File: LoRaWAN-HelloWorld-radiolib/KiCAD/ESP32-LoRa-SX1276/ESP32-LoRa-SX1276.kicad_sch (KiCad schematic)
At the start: 2 parts, among them U1 ESP32-DEVKITC-32UE, U2 SX1276

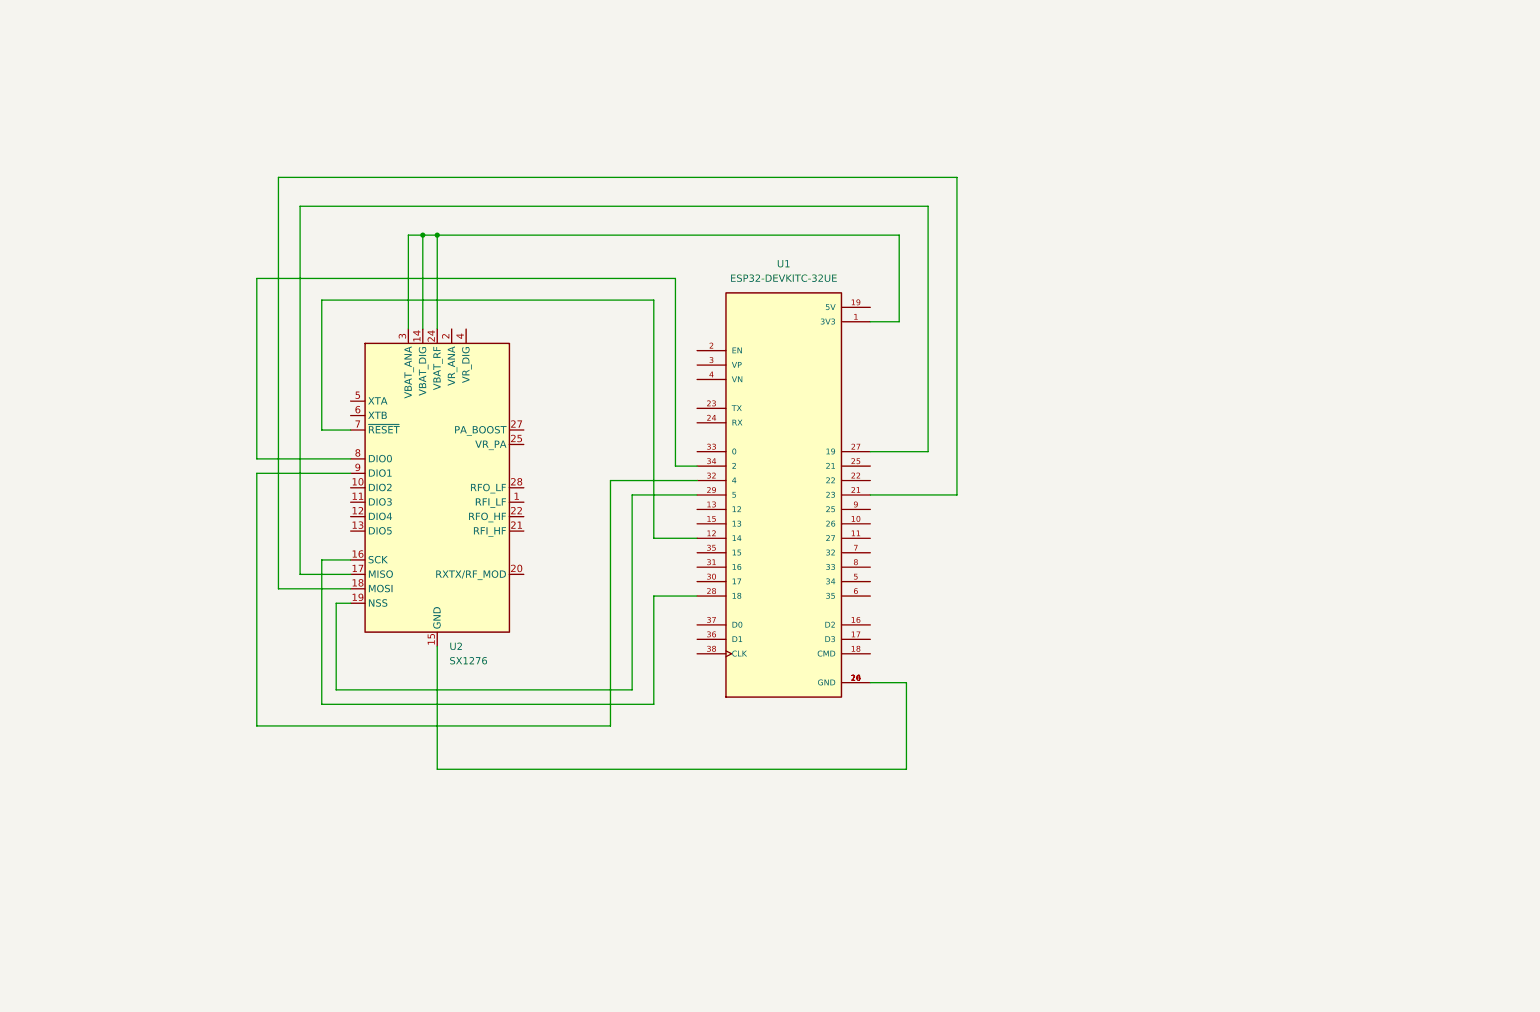
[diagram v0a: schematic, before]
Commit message: Roll back to full schema for SX1276 including all other sensors
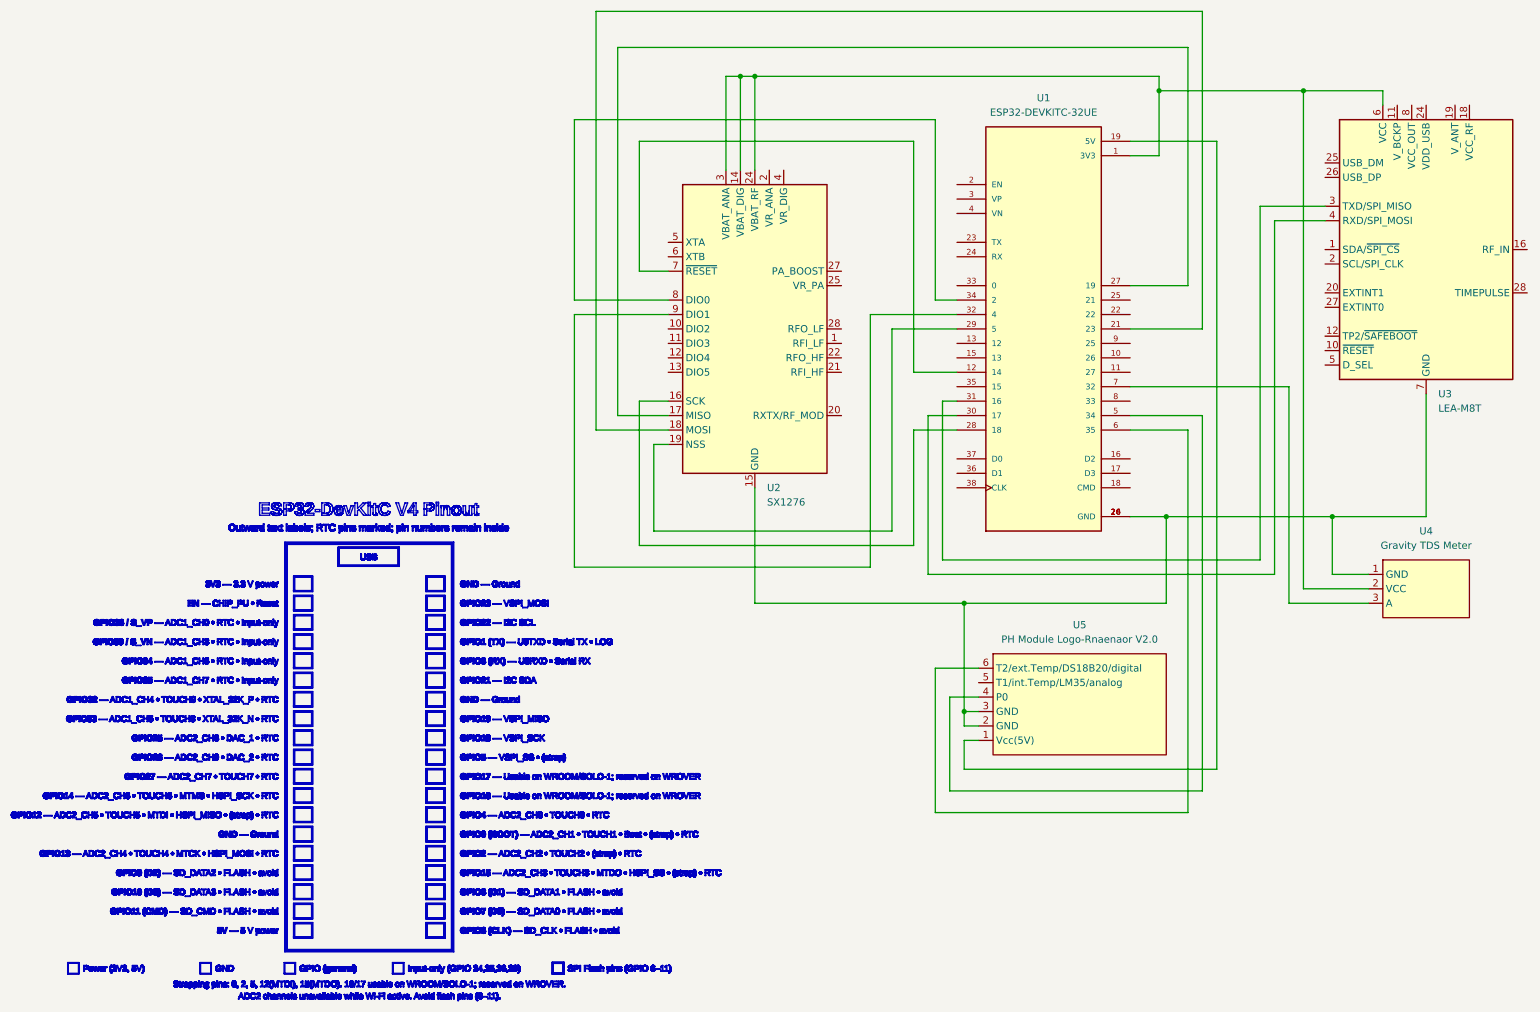
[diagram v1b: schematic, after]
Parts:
- added U3: LEA-M8T, RF_GPS:ublox_LEA, symbol RF_GPS:LEA-M8T
- added U4: Gravity TDS Meter, symbol AdditionalFromVoc:Gravity_TDS_Meter_V1.0
- added U5: PH Module Logo-Rnaenaor V2.0, symbol AdditionalFromVoc:PH_Module_Logo-Rnaenaor
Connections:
- net at U1.1 (3V3), U2.14 (VBAT_DIG), U2.24 (VBAT_RF)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: now also U3.6 (VCC), U4.2 (VCC)
- net at U1.14 (GND), U1.20 (GND), U1.26 (GND)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: now also U3.13 (GND), U3.14 (GND), U3.15 (GND), U3.17 (GND), U3.7 (GND), U4.1 (GND), U5.2 (GND), U5.3 (GND)
- net at U1.19 (5V): now also U5.1 (Vcc(5V))
- net at U1.30 (17): now also U3.4 (RXD/SPI_MOSI)
- net at U1.31 (16): now also U3.3 (TXD/SPI_MISO)
- net at U1.5 (34): now also U5.4 (P0)
- net at U1.6 (35): now also U5.6 (T2/ext.Temp/DS18B20/digital)
- net at U1.7 (32): now also U4.3 (A)
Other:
- moved on the sheet: U1, U2
